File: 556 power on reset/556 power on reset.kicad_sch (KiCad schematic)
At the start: 12 parts, among them J1 Conn_01x04_Socket, Q1 2N7002, U1 NA556

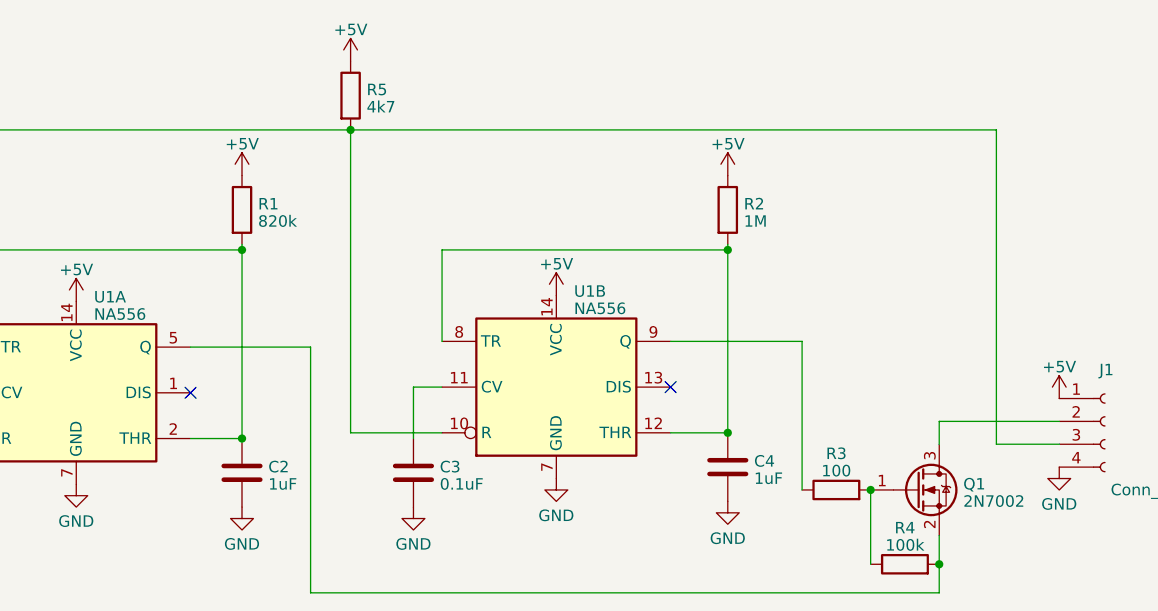
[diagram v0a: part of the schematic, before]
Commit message: update for bigger capacitors
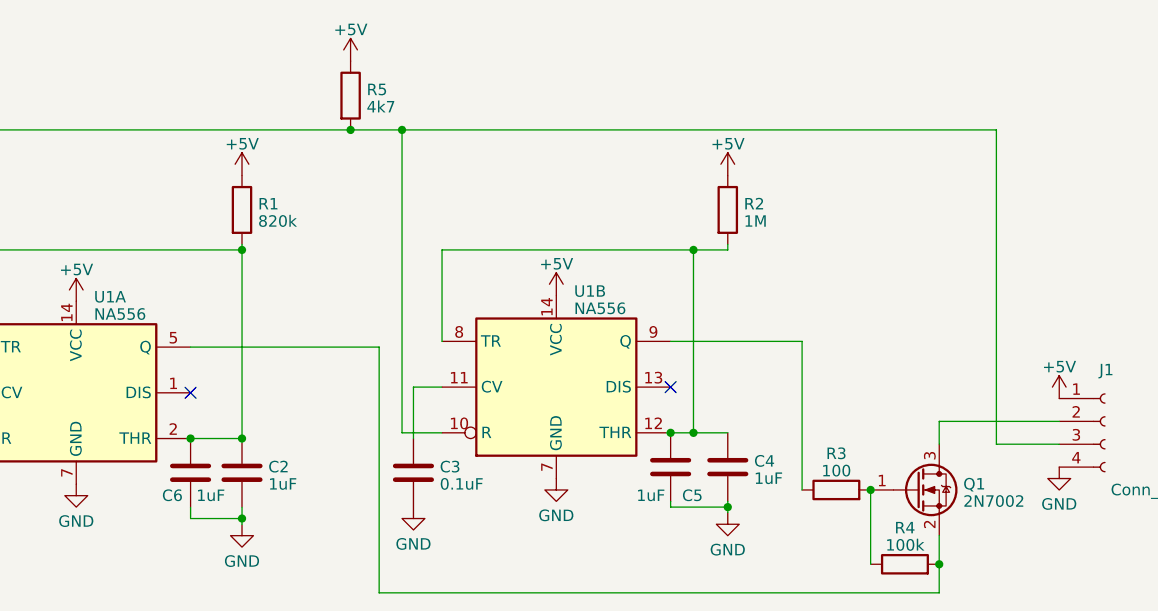
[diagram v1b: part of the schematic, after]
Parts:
- added C5, C6: 1uF, Evan's parts:V type tantalum, symbol Device:C
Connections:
- net GND: now also C5.2, C6.2
- net at C2.1, R1.2, U1.2 (THR)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: now also C6.1
- net at C4.1, R2.2, U1.12 (THR)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: now also C5.1
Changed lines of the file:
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@@
 (kicad_sch (version 20230121) (generator eeschema)
   (paper "A4")
+  (junction (at 135.89 60.96) (diameter 0) (color 0 0 0 0)
+  )
   (junction (at 88.265 40.64) (diameter 0) (color 0 0 0 0)
   )
@@
   (junction (at 88.265 61.595) (diameter 0) (color 0 0 0 0)
   )
-  (junction (at 142.24 40.64) (diameter 0) (color 0 0 0 0)
-  )
-  (junction (at 142.24 60.96) (diameter 0) (color 0 0 0 0)
+  (junction (at 142.24 69.215) (diameter 0) (color 0 0 0 0)
+  )
+  (junction (at 138.43 40.64) (diameter 0) (color 0 0 0 0)
   )
   (junction (at 100.33 27.305) (diameter 0) (color 0 0 0 0)
   )
   (junction (at 158.115 67.31) (diameter 0) (color 0 0 0 0)
+  )
+  (junction (at 138.43 60.96) (diameter 0) (color 0 0 0 0)
+  )
+  (junction (at 106.045 27.305) (diameter 0) (color 0 0 0 0)
+  )
+  (junction (at 82.55 61.595) (diameter 0) (color 0 0 0 0)
+  )
+  (junction (at 88.265 70.485) (diameter 0) (color 0 0 0 0)
   )
   (no_connect (at 135.89 55.88))
@@
     (stroke (width 0) (type default))
   )
+  (wire (pts (xy 138.43 60.96) (xy 142.24 60.96))
+    (stroke (width 0) (type default))
+  )
+  (wire (pts (xy 106.045 27.305) (xy 100.33 27.305))
+    (stroke (width 0) (type default))
+  )
   (wire (pts (xy 57.15 61.595) (xy 55.245 61.595))
     (stroke (width 0) (type default))
   )
-  (wire (pts (xy 110.49 40.64) (xy 142.24 40.64))
-    (stroke (width 0) (type default))
-  )
-  (wire (pts (xy 142.24 60.96) (xy 135.89 60.96))
-    (stroke (width 0) (type default))
-  )
-  (wire (pts (xy 142.24 40.64) (xy 142.24 60.96))
-    (stroke (width 0) (type default))
-  )
-  (wire (pts (xy 100.33 27.305) (xy 100.33 60.96))
+  (wire (pts (xy 110.49 40.64) (xy 138.43 40.64))
+    (stroke (width 0) (type default))
+  )
+  (wire (pts (xy 138.43 40.64) (xy 138.43 60.96))
+    (stroke (width 0) (type default))
+  )
+  (wire (pts (xy 106.045 27.305) (xy 106.045 60.96))
     (stroke (width 0) (type default))
   )
@@
     (stroke (width 0) (type default))
   )
-  (wire (pts (xy 95.885 51.435) (xy 82.55 51.435))
-    (stroke (width 0) (type default))
-  )
-  (wire (pts (xy 95.885 78.74) (xy 95.885 51.435))
+  (wire (pts (xy 103.505 51.435) (xy 82.55 51.435))
+    (stroke (width 0) (type default))
+  )
+  (wire (pts (xy 103.505 78.74) (xy 103.505 51.435))
+    (stroke (width 0) (type default))
+  )
+  (wire (pts (xy 142.24 69.215) (xy 142.24 68.58))
     (stroke (width 0) (type default))
   )
@@
     (stroke (width 0) (type default))
   )
+  (wire (pts (xy 138.43 60.96) (xy 135.89 60.96))
+    (stroke (width 0) (type default))
+  )
   (wire (pts (xy 88.265 40.64) (xy 88.265 61.595))
     (stroke (width 0) (type default))
   )
+  (wire (pts (xy 138.43 40.64) (xy 142.24 40.64))
+    (stroke (width 0) (type default))
+  )
+  (wire (pts (xy 135.89 68.58) (xy 135.89 69.215))
+    (stroke (width 0) (type default))
+  )
   (wire (pts (xy 150.495 50.8) (xy 150.495 67.31))
     (stroke (width 0) (type default))
   )
-  (wire (pts (xy 100.33 60.96) (xy 110.49 60.96))
-    (stroke (width 0) (type default))
-  )
-  (wire (pts (xy 165.735 78.74) (xy 95.885 78.74))
+  (wire (pts (xy 142.24 69.85) (xy 142.24 69.215))
+    (stroke (width 0) (type default))
+  )
+  (wire (pts (xy 82.55 70.485) (xy 88.265 70.485))
+    (stroke (width 0) (type default))
+  )
+  (wire (pts (xy 82.55 69.215) (xy 82.55 70.485))
+    (stroke (width 0) (type default))
+  )
+  (wire (pts (xy 106.045 60.96) (xy 110.49 60.96))
+    (stroke (width 0) (type default))
+  )
+  (wire (pts (xy 165.735 78.74) (xy 103.505 78.74))
     (stroke (width 0) (type default))
   )
@@
     (stroke (width 0) (type default))
   )
+  (wire (pts (xy 88.265 71.12) (xy 88.265 70.485))
+    (stroke (width 0) (type default))
+  )
   (wire (pts (xy 158.115 67.31) (xy 158.115 75.565))
     (stroke (width 0) (type default))
@@
     (stroke (width 0) (type default))
   )
-  (wire (pts (xy 172.085 27.305) (xy 100.33 27.305))
+  (wire (pts (xy 88.265 70.485) (xy 88.265 69.215))
+    (stroke (width 0) (type default))
+  )
+  (wire (pts (xy 172.085 27.305) (xy 106.045 27.305))
     (stroke (width 0) (type default))
   )
@@
   )
   (wire (pts (xy 179.07 62.23) (xy 172.085 62.23))
+    (stroke (width 0) (type default))
+  )
+  (wire (pts (xy 135.89 69.215) (xy 142.24 69.215))
     (stroke (width 0) (type default))
   )
@@
     )
   )
-  (symbol (lib_id "power:GND") (at 142.24 68.58 0) (unit 1)
-    (in_bom yes) (on_board yes) (dnp no) (fields_autoplaced)
-    (property "Reference" "#PWR013" (at 142.24 74.93 0)
-      (effects (font (size 1.27 1.27)) hide)
-    )
-    (property "Value" "GND" (at 142.24 72.7155 0)
-      (effects (font (size 1.27 1.27)))
-    )
-    (property "Footprint" "" (at 142.24 68.58 0)
-      (effects (font (size 1.27 1.27)) hide)
-    )
-    (property "Datasheet" "" (at 142.24 68.58 0)
+  (symbol (lib_id "power:GND") (at 142.24 69.85 0) (unit 1)
+    (in_bom yes) (on_board yes) (dnp no) (fields_autoplaced)
+    (property "Reference" "#PWR013" (at 142.24 76.2 0)
+      (effects (font (size 1.27 1.27)) hide)
+    )
+    (property "Value" "GND" (at 142.24 73.9855 0)
+      (effects (font (size 1.27 1.27)))
+    )
+    (property "Footprint" "" (at 142.24 69.85 0)
+      (effects (font (size 1.27 1.27)) hide)
+    )
+    (property "Datasheet" "" (at 142.24 69.85 0)
       (effects (font (size 1.27 1.27)) hide)
     )
@@
     )
   )
-  (symbol (lib_id "power:GND") (at 88.265 69.215 0) (unit 1)
-    (in_bom yes) (on_board yes) (dnp no) (fields_autoplaced)
-    (property "Reference" "#PWR014" (at 88.265 75.565 0)
-      (effects (font (size 1.27 1.27)) hide)
-    )
-    (property "Value" "GND" (at 88.265 73.3505 0)
-      (effects (font (size 1.27 1.27)))
-    )
-    (property "Footprint" "" (at 88.265 69.215 0)
-      (effects (font (size 1.27 1.27)) hide)
-    )
-    (property "Datasheet" "" (at 88.265 69.215 0)
+  (symbol (lib_id "power:GND") (at 88.265 71.12 0) (unit 1)
+    (in_bom yes) (on_board yes) (dnp no) (fields_autoplaced)
+    (property "Reference" "#PWR014" (at 88.265 77.47 0)
+      (effects (font (size 1.27 1.27)) hide)
+    )
+    (property "Value" "GND" (at 88.265 75.2555 0)
+      (effects (font (size 1.27 1.27)))
+    )
+    (property "Footprint" "" (at 88.265 71.12 0)
+      (effects (font (size 1.27 1.27)) hide)
+    )
+    (property "Datasheet" "" (at 88.265 71.12 0)
       (effects (font (size 1.27 1.27)) hide)
     )
@@
     )
   )
+  (symbol (lib_id "Device:C") (at 135.89 64.77 0) (unit 1)
+    (in_bom yes) (on_board yes) (dnp no)
+    (property "Reference" "C5" (at 137.16 67.945 0)
+      (effects (font (size 1.27 1.27)) (justify left))
+    )
+    (property "Value" "1uF" (at 132.08 67.945 0)
+      (effects (font (size 1.27 1.27)) (justify left))
+    )
+    (property "Footprint" "Evan's parts:V type tantalum" (at 136.8552 68.58 0)
+      (effects (font (size 1.27 1.27)) hide)
+    )
+    (property "Datasheet" "~" (at 135.89 64.77 0)
+      (effects (font (size 1.27 1.27)) hide)
+    )
+    (pin "1")
+    (pin "2")
+    (instances
+      (project "556 power on reset"
+        (path "/33ca6885-3d17-439a-b035-be16c7ebb0ed"
+          (reference "C5") (unit 1)
+        )
+      )
+    )
+  )
   (symbol (lib_id "power:+5V") (at 69.85 46.355 0) (unit 1)
     (in_bom yes) (on_board yes) (dnp no) (fields_autoplaced)
@@
         )
       )
+    )
+  )
+  (symbol (lib_id "Device:C") (at 82.55 65.405 0) (unit 1)
+    (in_bom yes) (on_board yes) (dnp no)
+    (property "Reference" "C6" (at 79.375 67.945 0)
+      (effects (font (size 1.27 1.27)) (justify left))
+    )
+    (property "Value" "1uF" (at 83.185 67.945 0)
+      (effects (font (size 1.27 1.27)) (justify left))
+    )
+    (property "Footprint" "Evan's parts:V type tantalum" (at 83.5152 69.215 0)
+      (effects (font (size 1.27 1.27)) hide)
+    )
+    (property "Datasheet" "~" (at 82.55 65.405 0)
+      (effects (font (size 1.27 1.27)) hide)
+    )
+    (pin "1")
+    (pin "2")
+    (instances
+      (project "556 power on reset"
+        (path "/33ca6885-3d17-439a-b035-be16c7ebb0ed"
+          (reference "C6") (unit 1)
+        )
+      )

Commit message: updates for manufacturing
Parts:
- C5, C6: value 1uF -> DNP
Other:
- moved on the sheet: C1, C2, C3, C4, C5, C6, J1, Q1, R1, R2, R3, R4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
